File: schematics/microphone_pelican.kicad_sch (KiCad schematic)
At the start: 4 parts, among them M1 MIC4013-X

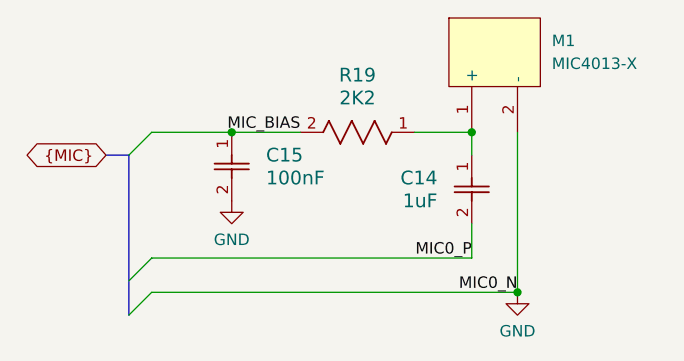
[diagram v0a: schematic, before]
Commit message: updated schematic based on review
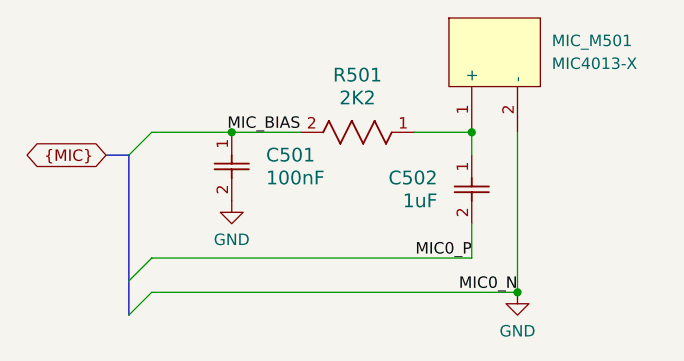
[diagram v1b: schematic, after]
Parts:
- renumbered C15 to C501, C14 to C502, M1 to MIC_M501, R19 to R501
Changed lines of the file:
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@@
 		(dnp no)
 		(fields_autoplaced yes)
-		(property "Reference" "R19"
+		(property "Reference" "R501"
 			(at 106.68 53.34 0)
 			(show_name no)
@@
 			(project "pelican"
 				(path "/03ccc822-2fac-4029-af97-539e9460fe35/4aa55629-72f0-42cd-91f0-be24c8a25a9f"
-					(reference "R19")
+					(reference "R501")
 					(unit 1)
 				)
@@
 		(dnp no)
 		(fields_autoplaced yes)
-		(property "Reference" "C15"
+		(property "Reference" "C501"
 			(at 96.52 62.2299 90)
 			(show_name no)
@@
 			(project "pelican"
 				(path "/03ccc822-2fac-4029-af97-539e9460fe35/4aa55629-72f0-42cd-91f0-be24c8a25a9f"
-					(reference "C15")
+					(reference "C501")
 					(unit 1)
 				)
@@
 		(in_pos_files yes)
 		(dnp no)
-		(property "Reference" "#PWR62"
+		(property "Reference" "#PWR0502"
 			(at 124.46 83.82 0)
 			(hide yes)
@@
 			(project "pelican"
 				(path "/03ccc822-2fac-4029-af97-539e9460fe35/4aa55629-72f0-42cd-91f0-be24c8a25a9f"
-					(reference "#PWR62")
+					(reference "#PWR0502")
 					(unit 1)
 				)
@@
 		(in_pos_files yes)
 		(dnp no)
-		(property "Reference" "C14"
+		(property "Reference" "C502"
 			(at 115.57 64.7699 90)
 			(show_name no)
@@
 			(project "pelican"
 				(path "/03ccc822-2fac-4029-af97-539e9460fe35/4aa55629-72f0-42cd-91f0-be24c8a25a9f"
-					(reference "C14")
+					(reference "C502")
 					(unit 1)
 				)
@@
 		(in_pos_files yes)
 		(dnp no)
-		(property "Reference" "#PWR63"
+		(property "Reference" "#PWR0501"
 			(at 92.71 73.66 0)
 			(hide yes)
@@
 			(project "pelican"
 				(path "/03ccc822-2fac-4029-af97-539e9460fe35/4aa55629-72f0-42cd-91f0-be24c8a25a9f"
-					(reference "#PWR63")
+					(reference "#PWR0501")
 					(unit 1)
 				)
@@
 		(dnp no)
 		(fields_autoplaced yes)
-		(property "Reference" "M1"
+		(property "Reference" "MIC_M501"
 			(at 128.27 49.5249 0)
 			(show_name no)
@@
 			(project "pelican"
 				(path "/03ccc822-2fac-4029-af97-539e9460fe35/4aa55629-72f0-42cd-91f0-be24c8a25a9f"
-					(reference "M1")
+					(reference "MIC_M501")
 					(unit 1)
 				)
